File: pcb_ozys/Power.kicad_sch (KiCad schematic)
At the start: 34 parts, among them J1 Conn_01x02_Pin, Q1 AO3401A, Q2 AO3401A, Q3 AO3401A, U2 TPS63070RNMR, U3 AMS1117-3.3

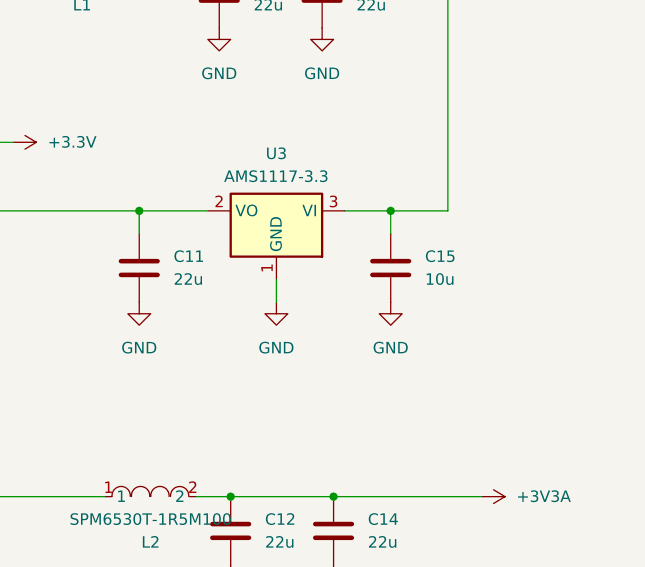
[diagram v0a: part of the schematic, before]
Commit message: Started PCBs fixed connectors
- Fixed Bypass on CAN
- Seperated SG connectors from 2x1 to 1x1
- Rough Draft of Epsilon
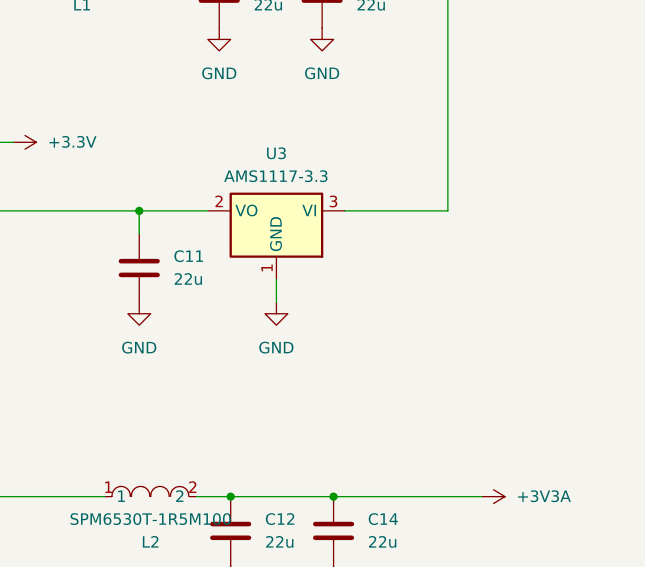
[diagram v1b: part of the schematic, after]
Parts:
- removed C15: 10u, Capacitor_SMD:C_0603_1608Metric, symbol Device:C
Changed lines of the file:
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@@
 	)
 	(junction
-		(at 238.76 78.74)
-		(diameter 0)
-		(color 0 0 0 0)
-	)
-	(junction
 		(at 129.54 107.95)
 		(diameter 0)
@@
 	(wire
 		(pts
-			(xy 238.76 78.74) (xy 245.11 78.74)
+			(xy 233.68 78.74) (xy 245.11 78.74)
 		)
 		(stroke
@@
 	(wire
 		(pts
-			(xy 233.68 78.74) (xy 238.76 78.74)
-		)
-		(stroke
-			(width 0)
-			(type default)
-		)
-	)
-	(wire
-		(pts
 			(xy 71.12 30.48) (xy 83.82 30.48)
 		)
@@
 	(wire
 		(pts
-			(xy 238.76 81.28) (xy 238.76 78.74)
-		)
-		(stroke
-			(width 0)
-			(type default)
-		)
-	)
-	(wire
-		(pts
 			(xy 104.14 53.34) (xy 93.98 53.34)
 		)
@@
 	)
 	(symbol
-		(lib_id "power:GND")
-		(at 238.76 88.9 0)
-		(unit 1)
-		(exclude_from_sim no)
-		(in_bom yes)
-		(on_board yes)
-		(dnp no)
-		(fields_autoplaced yes)
-		(property "Reference" "#PWR038"
-			(at 238.76 95.25 0)
-			(effects
-				(font
-					(size 1.27 1.27)
-				)
-				(hide yes)
-			)
-		)
-		(property "Value" "GND"
-			(at 238.76 93.98 0)
-			(effects
-				(font
-					(size 1.27 1.27)
-				)
-			)
-		)
-		(property "Footprint" ""
-			(at 238.76 88.9 0)
-			(effects
-				(font
-					(size 1.27 1.27)
-				)
-				(hide yes)
-			)
-		)
-		(property "Datasheet" ""
-			(at 238.76 88.9 0)
-			(effects
-				(font
-					(size 1.27 1.27)
-				)
-				(hide yes)
-			)
-		)
-		(property "Description" "Power symbol creates a global label with name \"GND\" , ground"
-			(at 238.76 88.9 0)
-			(effects
-				(font
-					(size 1.27 1.27)
-				)
-				(hide yes)
-			)
-		)
-		(pin "1"
-		)
-		(instances
-			(project "SG_PCB_V3_1"
-				(path "/c13c867e-6e7c-48dd-82ed-469b98ba6beb/f6677e1d-2e58-46fd-b64d-3824f7e6308f/3ee0415b-0594-46e5-9d72-ed6e84b019c6"
-					(reference "#PWR038")
-					(unit 1)
-				)
-			)
-		)
-	)
-	(symbol
 		(lib_id "Transistor_FET:AO3401A")
 		(at 55.88 93.98 270)
@@
 					(unit 1)
 				)
-			)
-		)
-	)
-	(symbol
-		(lib_id "Device:C")
-		(at 238.76 85.09 180)
-		(unit 1)
-		(exclude_from_sim no)
-		(in_bom yes)
-		(on_board yes)
-		(dnp no)
-		(fields_autoplaced yes)
-		(property "Reference" "C15"
-			(at 242.57 83.82 0)
-			(effects
-				(font
-					(size 1.27 1.27)
-				)
-				(justify right)
-			)
-		)
-		(property "Value" "10u"
-			(at 242.57 86.36 0)
-			(effects
-				(font
-					(size 1.27 1.27)
-				)
-				(justify right)
-			)
-		)
-		(property "Footprint" "Capacitor_SMD:C_0603_1608Metric"
-			(at 237.7948 81.28 0)
-			(effects
-				(font
-					(size 1.27 1.27)
-				)
-				(hide yes)
-			)
-		)
-		(property "Datasheet" "~"
-			(at 238.76 85.09 0)
-			(effects
-				(font
-					(size 1.27 1.27)
-				)
-				(hide yes)
-			)
-		)
-		(property "Description" "Unpolarized capacitor"
-			(at 238.76 85.09 0)
-			(effects
-				(font
-					(size 1.27 1.27)
-				)
-				(hide yes)
-			)
-		)
-		(pin "1"
-		)
-		(pin "2"
-		)
-		(instances
-			(project "SG_PCB_V3_1"
-				(path "/c13c867e-6e7c-48dd-82ed-469b98ba6beb/f6677e1d-2e58-46fd-b64d-3824f7e6308f/3ee0415b-0594-46e5-9d72-ed6e84b019c6"
-					(reference "C15")
-					(unit 1)
-				)

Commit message: Updated Epsilon PCB and Ozys Sch
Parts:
- removed Q2: AO3401A, Package_TO_SOT_SMD:SOT-23, symbol Transistor_FET:AO3401A
- removed R9: 150k, Resistor_SMD:R_0603_1608Metric, symbol Device:R
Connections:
- net VBUS: now reaches D1.2 (A), USB1.11 (VBUS), USB1.2 (VBUS)

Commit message: Yolo
Nothing could go wrong
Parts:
- renumbered L4 to L3
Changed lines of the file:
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@@
 		(dnp no)
 		(fields_autoplaced yes)
-		(property "Reference" "L4"
+		(property "Reference" "L3"
 			(at 95.25 46.9899 90)
 			(effects
@@
 		(pin "1"
 		)
-		(instances
-			(project ""
-				(path "/c13c867e-6e7c-48dd-82ed-469b98ba6beb/f6677e1d-2e58-46fd-b64d-3824f7e6308f/3ee0415b-0594-46e5-9d72-ed6e84b019c6"
-					(reference "L4")
-					(unit 1)
-				)
-			)
-		)
+		(instances)
 	)
 	(symbol
